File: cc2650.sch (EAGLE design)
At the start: 25 parts, among them IC1 TPS73133DBVR, IC4 CC2650MODAMOHR, K1 CPC1117N, SW1 SPST_TACT-KMR2, SW3 SPST_TACT-KMR2

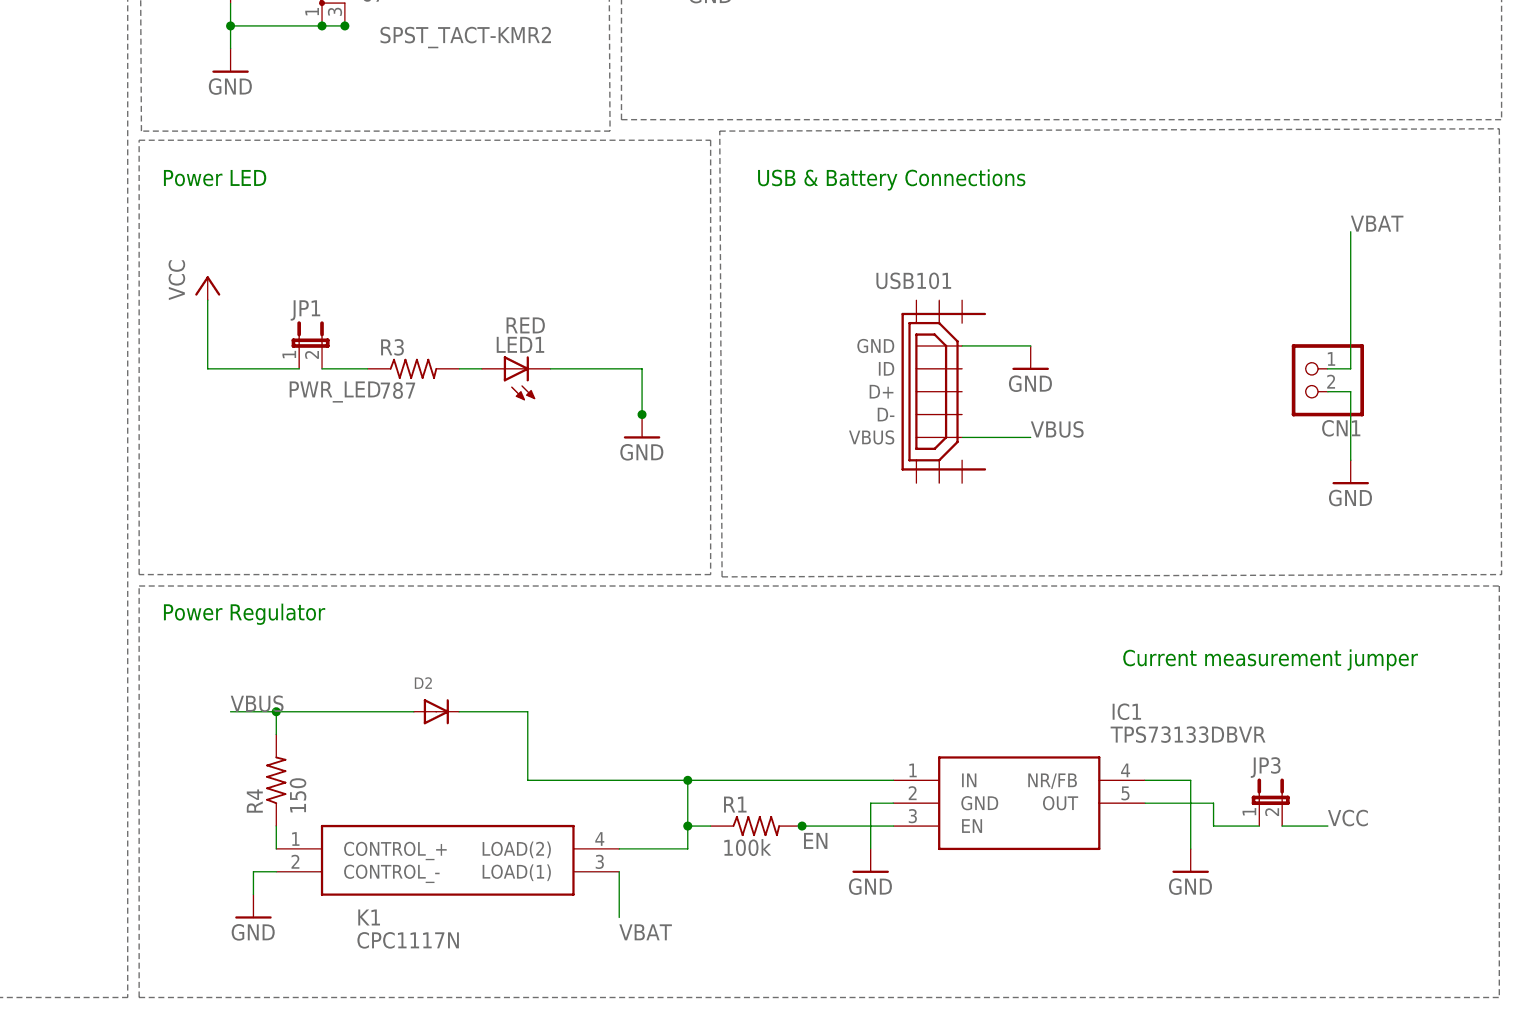
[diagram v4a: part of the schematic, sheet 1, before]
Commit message: Changed power circuitry. Added TI ESD Suppresor.
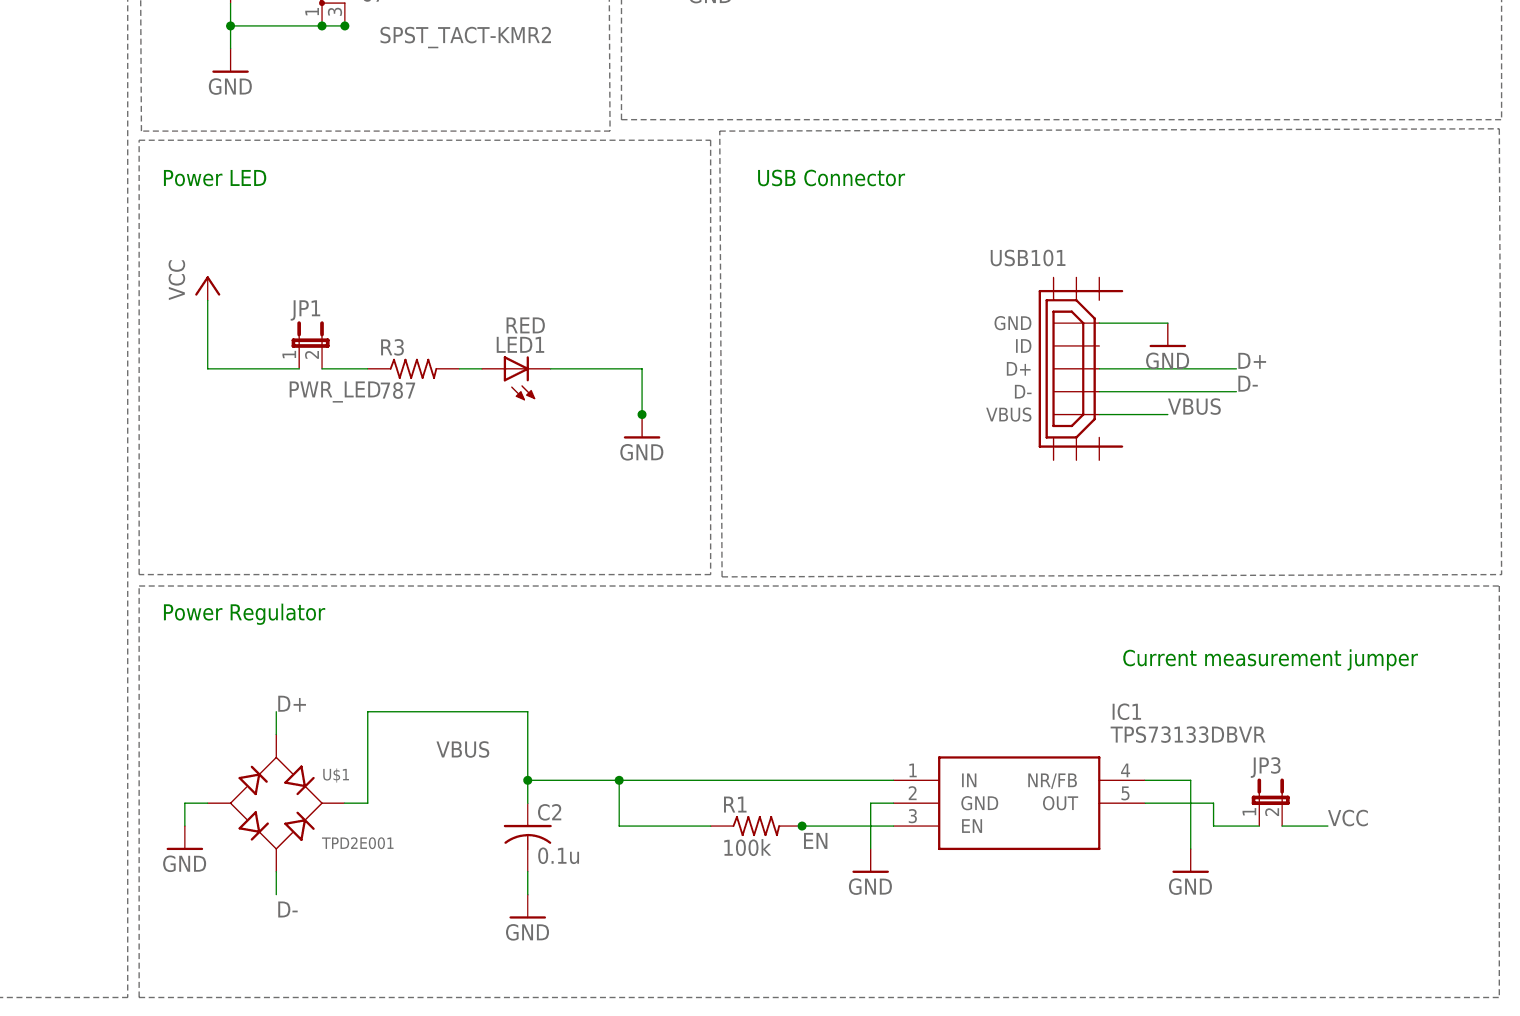
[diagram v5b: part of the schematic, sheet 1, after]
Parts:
- removed CN1: (no value), adafruit:JST_2PIN-THM-RA
- removed D2: (no value), adafruit:DIODE_SOD-123FL
- removed K1: CPC1117N, CPC1117N:CPC1117N
- removed R4: 150, adafruit:R-US_R1206
- added C2: 0.1u, adafruit:C-USC1206
- added U$1: TPD2E001, AMP_Ruler-LT1370:TPD2E001
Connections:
- removed net N$4: D2.C, IC1.IN, K1.LOAD(2), R1.1
- removed net N$6: K1.CONTROL_+, R4.1
- new net D+: U$1.AC1, USB101.D+
- new net D-: U$1.AC2, USB101.D-
- net GND: now also C2.2, U$1.-; no longer CN1.1, K1.CONTROL_-
- net VBAT: no longer CN1.2, K1.LOAD(1)
- net VBUS: now also C2.1, IC1.IN, R1.1, U$1.+; no longer D2.A, R4.2
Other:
- note added: "USB Connector"
- note removed: "USB & Battery Connections"
- moved on the sheet: USB101

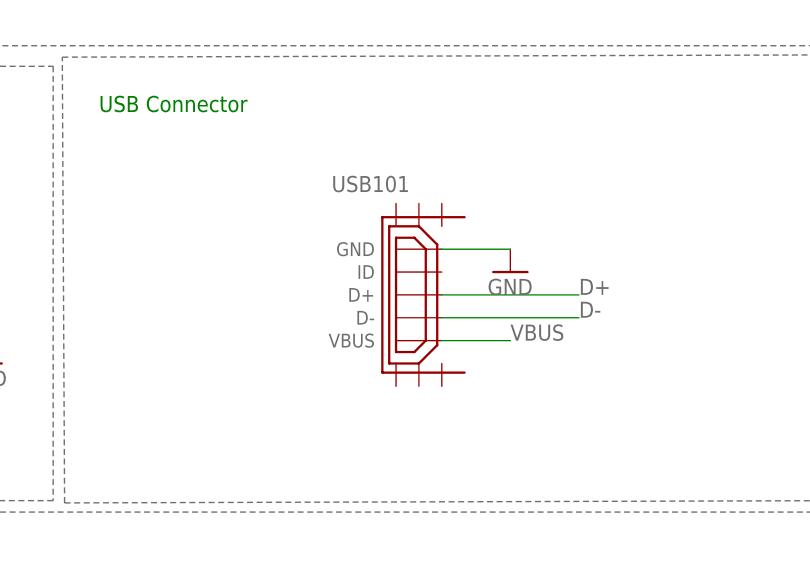
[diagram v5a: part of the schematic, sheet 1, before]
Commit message: changed usb to AMP lab part.
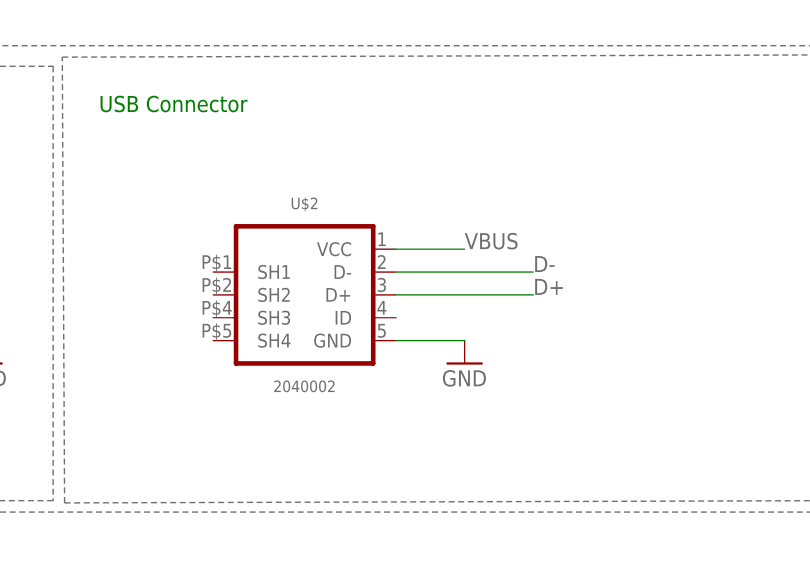
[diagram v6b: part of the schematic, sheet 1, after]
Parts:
- removed USB101: (no value), MSP_Connectors:USB-MICRO
- added U$2: 2040002, AMP_Ruler-LT1370:2040002
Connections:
- net D+: no longer USB101.D+
- net D-: no longer USB101.D-
- net GND: no longer USB101.GND
- net VBUS: no longer USB101.VBUS
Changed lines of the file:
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@@
 <part name="P+5" library="supply1" library_urn="urn:adsk.eagle:library:371" deviceset="VCC" device=""/>
 <part name="GND4" library="supply1" library_urn="urn:adsk.eagle:library:371" deviceset="GND" device=""/>
-<part name="USB101" library="MSP_Connectors" deviceset="USB-MICRO" device="">
-<attribute name="MF" value=""/>
-<attribute name="MPN" value="105164-0001"/>
-<attribute name="OC_NEWARK" value="99Y3224"/>
-</part>
 <part name="IC1" library="TPS73133DBVR" deviceset="TPS73133DBVR" device="">
 <attribute name="MF" value=""/>
@@
 </part>
 <part name="GND6" library="supply1" deviceset="GND" device=""/>
+<part name="U$2" library="AMP_Ruler-LT1370" deviceset="2040002" device=""/>
 </parts>
 <sheets>
@@
 <instance part="P+4" gate="VCC" x="-17.78" y="7.62"/>
 <instance part="P+5" gate="VCC" x="22.86" y="81.28"/>
-<instance part="GND4" gate="1" x="127" y="17.78"/>
-<instance part="USB101" gate="G$1" x="114.3" y="15.24" smashed="yes" rot="R180">
-<attribute name="NAME" x="115.824" y="28.448" size="1.778" layer="95" font="vector" rot="R180"/>
-<attribute name="VALUE" x="122.682" y="0.762" size="1.778" layer="96" font="vector" rot="R180"/>
-<attribute name="OC_NEWARK" x="114.3" y="15.24" size="1.778" layer="96" display="off"/>
-<attribute name="MF" x="114.3" y="15.24" size="1.778" layer="96" display="off"/>
-<attribute name="MPN" x="114.3" y="15.24" size="1.778" layer="96" display="off"/>
-</instance>
+<instance part="GND4" gate="1" x="121.92" y="7.62"/>
 <instance part="IC1" gate="G$1" x="96.52" y="-30.48">
 <attribute name="OC_NEWARK" x="96.52" y="-30.48" size="1.778" layer="96" display="off"/>
@@
 </instance>
 <instance part="GND6" gate="1" x="55.88" y="-45.72"/>
+<instance part="U$2" gate="G$1" x="106.68" y="15.24" rot="MR0"/>
 </instances>
 <busses>
@@
 </segment>
 <segment>
-<pinref part="USB101" gate="G$1" pin="GND"/>
 <pinref part="GND4" gate="1" pin="GND"/>
-<wire x1="119.38" y1="20.32" x2="127" y2="20.32" width="0.1524" layer="91"/>
+<wire x1="114.3" y1="10.16" x2="121.92" y2="10.16" width="0.1524" layer="91"/>
 </segment>
 <segment>
@@
 <net name="VBUS" class="2">
 <segment>
-<pinref part="USB101" gate="G$1" pin="VBUS"/>
-<wire x1="119.38" y1="10.16" x2="127" y2="10.16" width="0.1524" layer="91"/>
-<label x="127" y="10.16" size="1.778" layer="95"/>
+<wire x1="114.3" y1="20.32" x2="121.92" y2="20.32" width="0.1524" layer="91"/>
+<label x="121.92" y="20.32" size="1.778" layer="95"/>
 </segment>
 <segment>
@@
 <net name="D-" class="0">
 <segment>
-<pinref part="USB101" gate="G$1" pin="D-"/>
-<wire x1="119.38" y1="12.7" x2="134.62" y2="12.7" width="0.1524" layer="91"/>
-<label x="134.62" y="12.7" size="1.778" layer="95"/>
+<wire x1="114.3" y1="17.78" x2="129.54" y2="17.78" width="0.1524" layer="91"/>
+<label x="129.54" y="17.78" size="1.778" layer="95"/>
 </segment>
 <segment>
@@
 <net name="D+" class="0">
 <segment>
-<pinref part="USB101" gate="G$1" pin="D+"/>
-<wire x1="119.38" y1="15.24" x2="134.62" y2="15.24" width="0.1524" layer="91"/>
-<label x="134.62" y="15.24" size="1.778" layer="95"/>
-</segment>
-<segment>
+<wire x1="114.3" y1="15.24" x2="129.54" y2="15.24" width="0.1524" layer="91"/>
+<label x="129.54" y="15.24" size="1.778" layer="95"/>
+</segment>
+<segment>

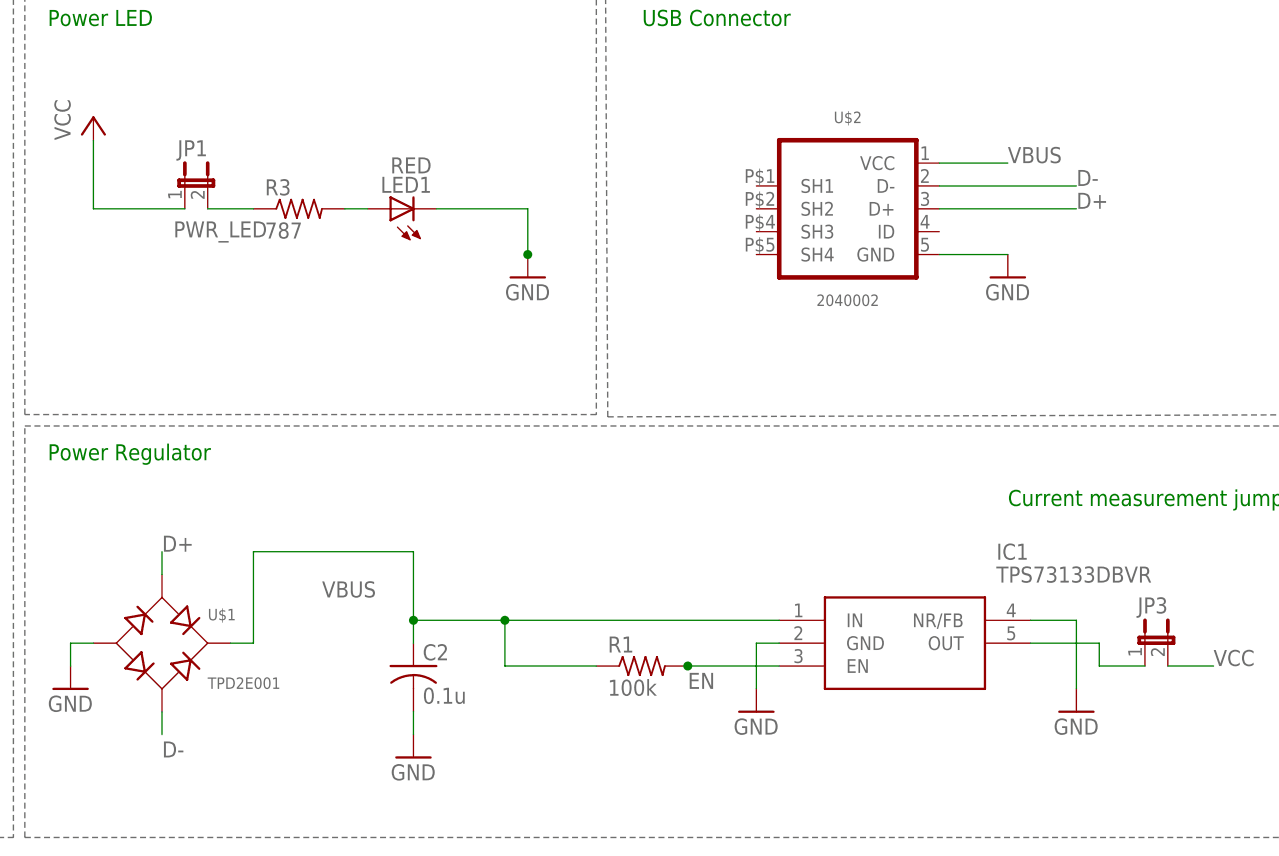
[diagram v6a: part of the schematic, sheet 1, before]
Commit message: changed USB circuit to closer match layout of AMP card.
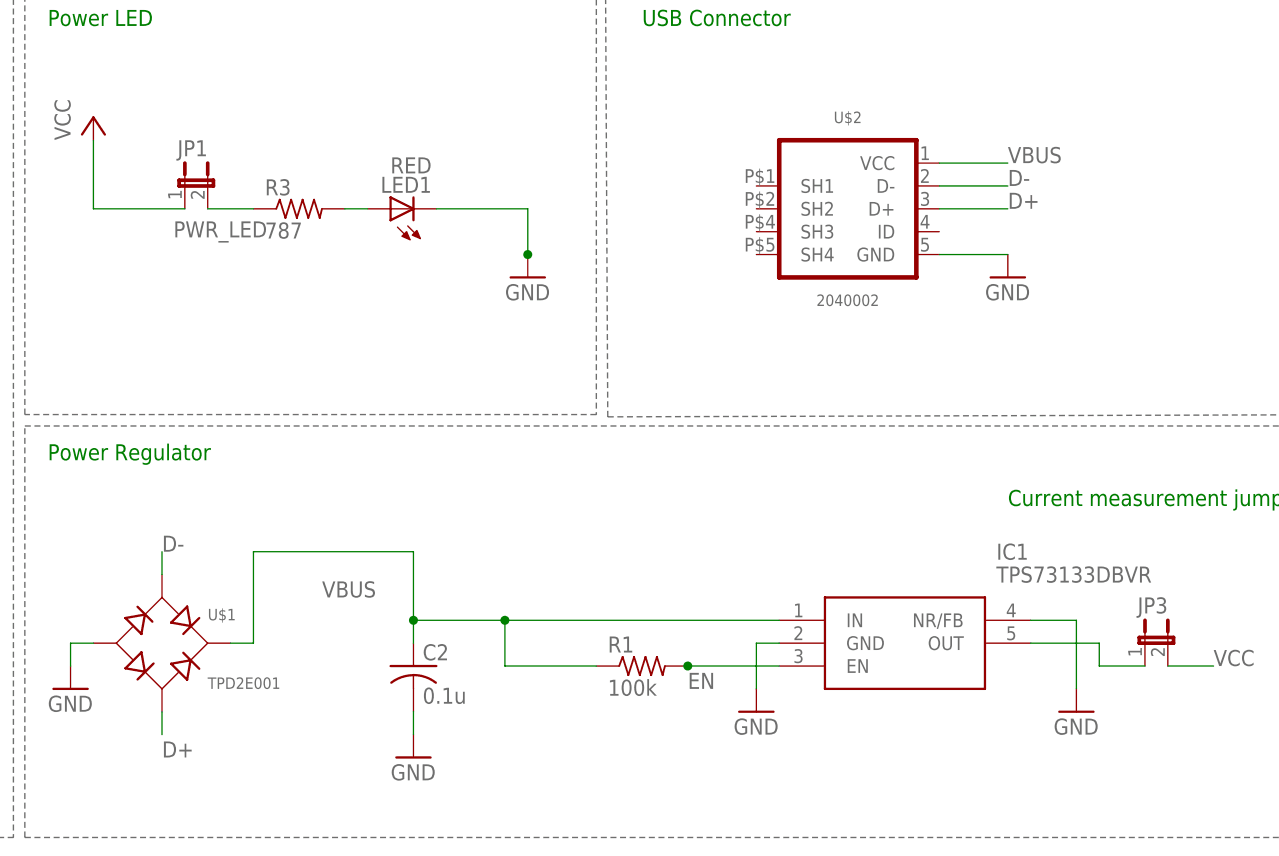
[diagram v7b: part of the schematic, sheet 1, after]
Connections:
- net D+: now also U$1.AC2, U$2.D+; no longer U$1.AC1
- net D-: now also U$1.AC1, U$2.D-; no longer U$1.AC2
- net GND: now also U$2.GND
- net VBUS: now also U$2.VCC
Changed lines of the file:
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@@
-</segment>
-<segment>
-<pinref part="GND4" gate="1" pin="GND"/>
-<wire x1="114.3" y1="10.16" x2="121.92" y2="10.16" width="0.1524" layer="91"/>
 </segment>
 <segment>
@@
 <pinref part="C2" gate="G$1" pin="2"/>
 <wire x1="55.88" y1="-43.18" x2="55.88" y2="-40.64" width="0.1524" layer="91"/>
+</segment>
+<segment>
+<pinref part="U$2" gate="G$1" pin="GND"/>
+<pinref part="GND4" gate="1" pin="GND"/>
+<wire x1="114.3" y1="10.16" x2="121.92" y2="10.16" width="0.1524" layer="91"/>
 </segment>
 </net>
@@
 </net>
 <net name="VBUS" class="2">
-<segment>
-<wire x1="114.3" y1="20.32" x2="121.92" y2="20.32" width="0.1524" layer="91"/>
-<label x="121.92" y="20.32" size="1.778" layer="95"/>
-</segment>
 <segment>
 <pinref part="MS1" gate="G$1" pin="USB"/>
@@
 <junction x="55.88" y="-30.48"/>
 </segment>
+<segment>
+<pinref part="U$2" gate="G$1" pin="VCC"/>
+<wire x1="114.3" y1="20.32" x2="121.92" y2="20.32" width="0.1524" layer="91"/>
+<label x="121.92" y="20.32" size="1.778" layer="95"/>
+</segment>
 </net>
 <net name="EN" class="0">
@@
 <net name="D-" class="0">
 <segment>
-<wire x1="114.3" y1="17.78" x2="129.54" y2="17.78" width="0.1524" layer="91"/>
-<label x="129.54" y="17.78" size="1.778" layer="95"/>
+<pinref part="U$2" gate="G$1" pin="D-"/>
+<wire x1="114.3" y1="17.78" x2="121.92" y2="17.78" width="0.1524" layer="91"/>
+<label x="121.92" y="17.78" size="1.778" layer="95"/>
+</segment>
+<segment>
+<pinref part="U$1" gate="G$1" pin="AC1"/>
+<wire x1="27.94" y1="-25.4" x2="27.94" y2="-22.86" width="0.1524" layer="91"/>
+<label x="27.94" y="-22.86" size="1.778" layer="95"/>
+</segment>
+</net>
+<net name="D+" class="0">
+<segment>
+<pinref part="U$2" gate="G$1" pin="D+"/>
+<wire x1="114.3" y1="15.24" x2="121.92" y2="15.24" width="0.1524" layer="91"/>
+<label x="121.92" y="15.24" size="1.778" layer="95"/>
 </segment>
 <segment>
@@
 </segment>
 </net>
-<net name="D+" class="0">
-<segment>
-<wire x1="114.3" y1="15.24" x2="129.54" y2="15.24" width="0.1524" layer="91"/>
-<label x="129.54" y="15.24" size="1.778" layer="95"/>
-</segment>
-<segment>
-<pinref part="U$1" gate="G$1" pin="AC1"/>
-<wire x1="27.94" y1="-25.4" x2="27.94" y2="-22.86" width="0.1524" layer="91"/>
-<label x="27.94" y="-22.86" size="1.778" layer="95"/>
-</segment>
-</net>
